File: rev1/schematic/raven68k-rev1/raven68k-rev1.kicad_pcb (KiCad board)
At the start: 4 copper layers, 203.2 x 114.3 mm, 77 parts, among them IC1 L5970D013TR, IC2 L5970D013TR, J1 CPLD_JTAG, J2 DUART_IO, J3 RAPC722BK, SW1 RESET_SW, U1 MCP100-465D, U10 28C256, U11 28C256, U2 68010D, U3 XC9572XL-VQ44, U4 68681, U5 74LS373, U6 CONSOLE, U7 DS12887+, U8 KM684000BLP-7L, U9 KM684000BLP-7L, X1 CLOCK, X2 CXO_DIP14

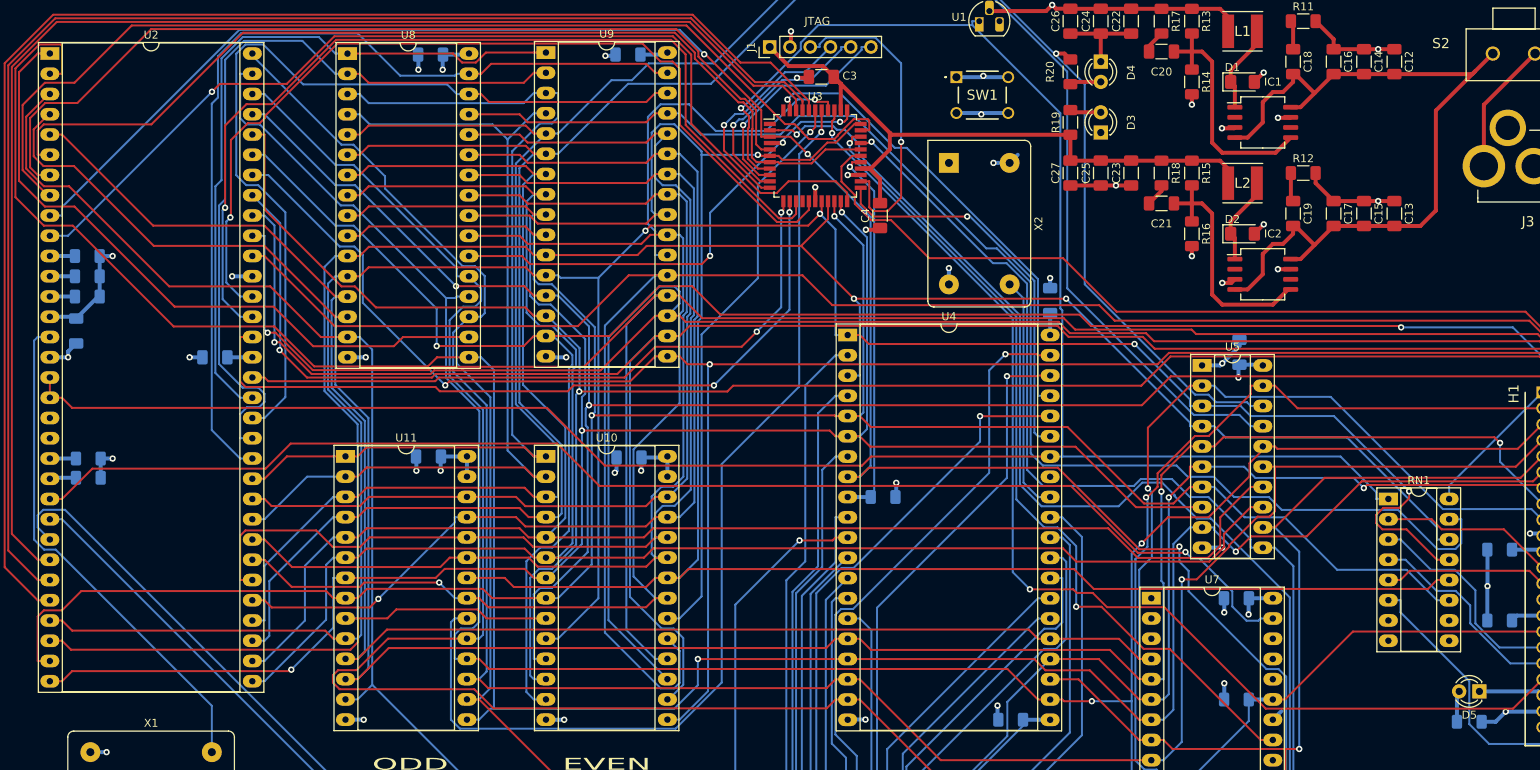
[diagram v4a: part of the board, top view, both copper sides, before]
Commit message: remove tiny leftover traces
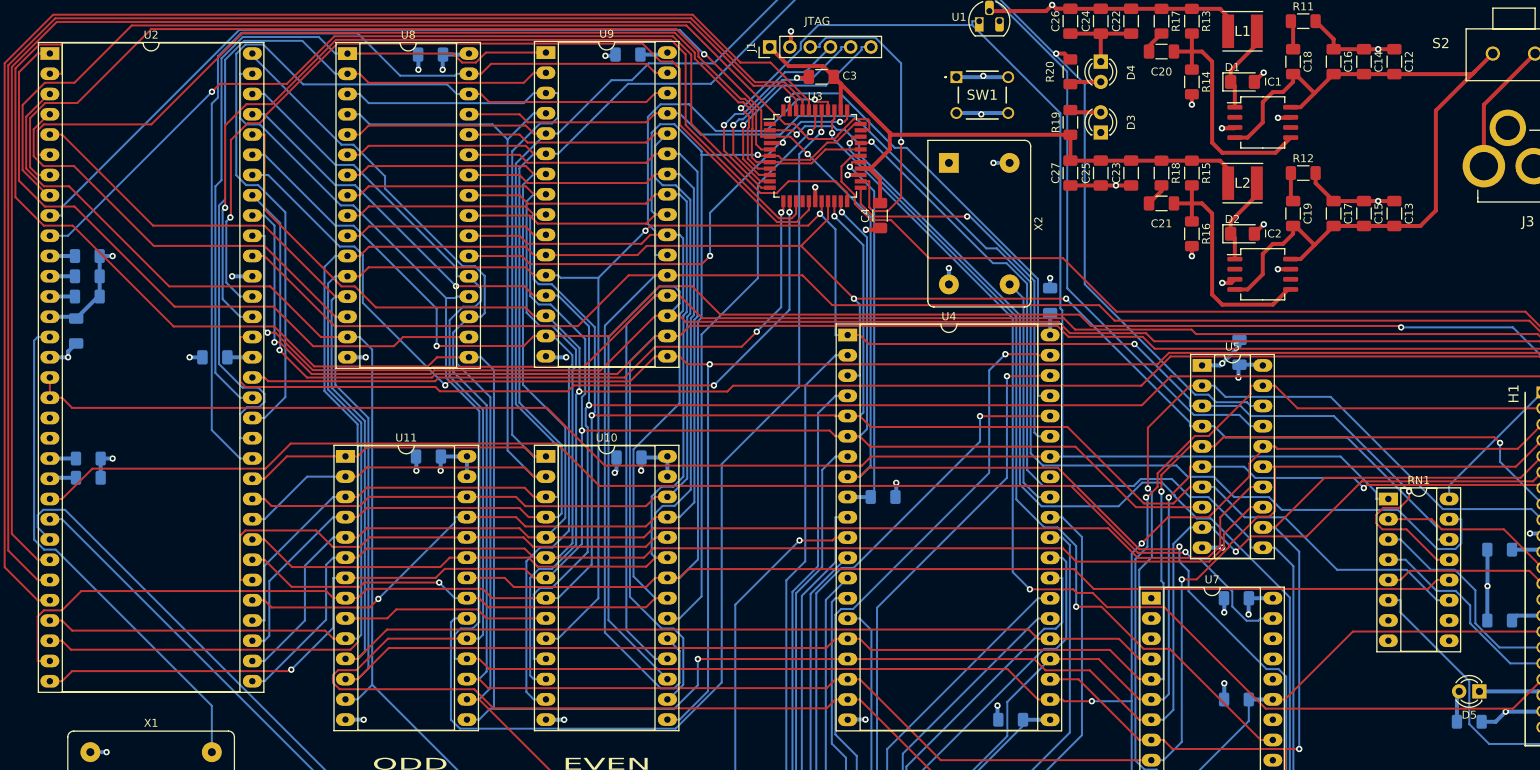
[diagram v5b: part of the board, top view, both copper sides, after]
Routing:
- net +5V: track 133.5 -> 127.0 mm
- net GND: track 147.4 -> 146.6 mm
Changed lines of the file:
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@@
       (layer "B.Cu" (type "copper") (thickness 0.035))
       (layer "B.Mask" (type "Bottom Solder Mask") (thickness 0.01))
+      (layer "B.Paste" (type "Bottom Solder Paste"))
+      (layer "B.SilkS" (type "Bottom Silk Screen"))
       (copper_finish "None")
       (dielectric_constraints no)
@@
       (drillshape 0)
       (scaleselection 1)
-      (outputdirectory "")
+      (outputdirectory "/home/ccureau/git/jani/Raven68k/rev1/gerber/")
     )
   )
@@
   (segment (start 193.0427 74.742) (end 194.173 74.742) (width 0.5) (layer "F.Cu") (net 22))
   (segment (start 173.99 43.4725) (end 177.8 43.4725) (width 0.5) (layer "F.Cu") (net 22))
-  (segment (start 207.29 64.1975) (end 207.01 64.4775) (width 0.5) (layer "F.Cu") (net 22))
   (segment (start 137.871 57.201) (end 137.922 57.15) (width 0.5) (layer "F.Cu") (net 22))
   (segment (start 179.705 62.5225) (end 181.61 62.5225) (width 0.5) (layer "F.Cu") (net 22))
@@
   (via blind (at 68.834 73.914) (size 0.8) (drill 0.4) (layers "In1.Cu" "B.Cu") (net 22))
   (via blind (at 63.5 84.074) (size 0.8) (drill 0.4) (layers "In1.Cu" "B.Cu") (net 22))
-  (segment (start 162.651 53.431) (end 162.814 53.594) (width 0.5) (layer "In2.Cu") (net 22))
-  (segment (start 162.977 53.431) (end 162.814 53.594) (width 0.5) (layer "In2.Cu") (net 22))
   (segment (start 159.691 53.431) (end 162.651 53.431) (width 0.5) (layer "B.Cu") (net 22))
   (segment (start 48.26 84.074) (end 45.979 84.074) (width 0.5) (layer "B.Cu") (net 22))
@@
   (via blind (at 171.704 39.878) (size 0.8) (drill 0.4) (layers "F.Cu" "In2.Cu") (net 25))
   (via blind (at 172.212 45.974) (size 0.8) (drill 0.4) (layers "F.Cu" "In2.Cu") (net 25))
-  (segment (start 163.231 48.931) (end 163.068 48.768) (width 0.5) (layer "In2.Cu") (net 25))
-  (segment (start 162.905 48.931) (end 163.068 48.768) (width 0.5) (layer "In2.Cu") (net 25))
   (via blind (at 164.338 59.69) (size 0.8) (drill 0.4) (layers "In2.Cu" "B.Cu") (net 25))
   (via blind (at 193.294 124.968) (size 0.8) (drill 0.4) (layers "In2.Cu" "B.Cu") (net 25))
@@
   (via blind (at 226.314 112.776) (size 0.8) (drill 0.4) (layers "In2.Cu" "B.Cu") (net 25))
   (segment (start 166.191 48.931) (end 163.231 48.931) (width 0.5) (layer "B.Cu") (net 25))
-  (segment (start 226.648 117.454) (end 226.288 117.094) (width 0.5) (layer "B.Cu") (net 25))
   (segment (start 120.054 46.101) (end 123.185 46.101) (width 0.5) (layer "B.Cu") (net 25))
-  (segment (start 120.054 45.5045) (end 120.054 46.101) (width 0.5) (layer "B.Cu") (net 25))
   (segment (start 196.342 114.338) (end 196.38 114.3) (width 0.5) (layer "B.Cu") (net 25))
   (segment (start 196.3805 114.3) (end 199.38 114.3) (width 0.5) (layer "B.Cu") (net 25))
   (segment (start 233.138 128.524) (end 233.188 128.474) (width 0.5) (layer "B.Cu") (net 25))
-  (segment (start 167.391 58.6695) (end 166.37 59.69) (width 0.5) (layer "B.Cu") (net 25))
   (segment (start 233.188 128.474) (end 235.188 128.474) (width 0.5) (layer "B.Cu") (net 25))
-  (segment (start 49.0555 78.989) (end 49.276 79.2095) (width 0.5) (layer "B.Cu") (net 25))
   (segment (start 227.33 129.794) (end 228.6 128.524) (width 0.5) (layer "B.Cu") (net 25))
   (segment (start 195.072 86.614) (end 195.072 85.1285) (width 0.5) (layer "B.Cu") (net 25))
   (segment (start 152.146 101.499) (end 152.045 101.6) (width 0.5) (layer "B.Cu") (net 25))
   (segment (start 196.342 116.332) (end 196.342 114.338) (width 0.5) (layer "B.Cu") (net 25))
-  (segment (start 184.145 114.295) (end 184.728 114.295) (width 0.5) (layer "B.Cu") (net 25))
   (segment (start 71.369 84.074) (end 71.374 84.069) (width 0.5) (layer "B.Cu") (net 25))
-  (segment (start 199.385 129.535) (end 200.451 128.469) (width 0.5) (layer "B.Cu") (net 25))
-  (segment (start 45.979 78.994) (end 45.974 78.989) (width 0.5) (layer "B.Cu") (net 25))
-  (segment (start 120.054 46.101) (end 120.18 46.228) (width 0.5) (layer "B.Cu") (net 25))
   (segment (start 95.0345 96.52) (end 98.278 96.52) (width 0.5) (layer "B.Cu") (net 25))
   (segment (start 98.42 46.101) (end 98.547 45.974) (width 0.5) (layer "B.Cu") (net 25))
   (segment (start 52.0315 76.454) (end 49.276 79.2095) (width 0.5) (layer "B.Cu") (net 25))
-  (segment (start 49.276 79.2095) (end 49.4675 79.2095) (width 0.5) (layer "B.Cu") (net 25))
   (segment (start 226.314 108.23) (end 226.288 108.204) (width 0.5) (layer "B.Cu") (net 25))
   (segment (start 195.199 85.0015) (end 198.036 85.0015) (width 0.5) (layer "B.Cu") (net 25))
@@
   (segment (start 52.223 76.454) (end 52.0315 76.454) (width 0.5) (layer "B.Cu") (net 25))
   (segment (start 226.314 112.776) (end 226.314 108.23) (width 0.5) (layer "B.Cu") (net 25))
-  (segment (start 120.054 46.101) (end 120.0535 46.101) (width 0.5) (layer "B.Cu") (net 25))
   (segment (start 152.146 99.822) (end 152.146 101.499) (width 0.5) (layer "B.Cu") (net 25))
   (segment (start 164.338 59.69) (end 166.37 59.69) (width 0.5) (layer "B.Cu") (net 25))
   (segment (start 171.45 78.5245) (end 171.45 81.285) (width 0.5) (layer "B.Cu") (net 25))
   (segment (start 120.1805 96.647) (end 123.297 96.647) (width 0.5) (layer "B.Cu") (net 25))
-  (segment (start 171.445 81.28) (end 171.45 81.285) (width 0.5) (layer "B.Cu") (net 25))
   (segment (start 193.294 124.968) (end 193.294 126.974) (width 0.5) (layer "B.Cu") (net 25))
   (segment (start 94.996 96.5585) (end 95.0345 96.52) (width 0.5) (layer "B.Cu") (net 25))
@@
   (segment (start 52.223 71.374) (end 53.848 71.374) (width 0.5) (layer "B.Cu") (net 25))
   (segment (start 196.38 114.3) (end 196.3805 114.3) (width 0.5) (layer "B.Cu") (net 25))
-  (segment (start 120.142 46.1895) (end 120.054 46.101) (width 0.5) (layer "B.Cu") (net 25))
   (segment (start 52.223 71.374) (end 52.223 73.914) (width 0.5) (layer "B.Cu") (net 25))
-  (segment (start 199.385 114.295) (end 199.78 113.9) (width 0.5) (layer "B.Cu") (net 25))
   (segment (start 199.38 114.3) (end 199.385 114.295) (width 0.5) (layer "B.Cu") (net 25))
   (segment (start 164.846 129.439) (end 164.947 129.54) (width 0.5) (layer "B.Cu") (net 25))
@@
   (segment (start 159.691 48.931) (end 162.905 48.931) (width 0.5) (layer "B.Cu") (net 25))
   (segment (start 52.35 99.187) (end 52.35 96.774) (width 0.5) (layer "B.Cu") (net 25))
-  (segment (start 45.969 78.994) (end 45.974 78.989) (width 0.5) (layer "B.Cu") (net 25))
   (segment (start 120.18 98.2595) (end 120.18 96.647) (width 0.5) (layer "B.Cu") (net 25))
   (segment (start 45.974 78.989) (end 49.0555 78.989) (width 0.5) (layer "B.Cu") (net 25))
@@
   (segment (start 150.114 64.7315) (end 150.114 61.705) (width 0.5) (layer "F.Cu") (net 66))
   (segment (start 189.23 59.41) (end 185.42 59.41) (width 0.5) (layer "F.Cu") (net 66))
-  (segment (start 173.837 56.007) (end 173.99 56.16) (width 0.5) (layer "F.Cu") (net 66))
   (segment (start 148.81 60.401) (end 148.936 60.401) (width 0.5) (layer "F.Cu") (net 66))
   (segment (start 173.99 59.3975) (end 173.99 56.16) (width 0.5) (layer "F.Cu") (net 66))
@@
   (segment (start 201.65 64.1975) (end 201.93 64.4775) (width 0.5) (layer "F.Cu") (net 82))
   (segment (start 201.65 60.96) (end 201.65 64.1975) (width 0.5) (layer "F.Cu") (net 82))
-  (segment (start 186.982 45.72) (end 186.9825 45.72) (width 0.5) (layer "F.Cu") (net 83))
   (segment (start 189.23 43.46) (end 189.23 45.72) (width 0.5) (layer "F.Cu") (net 83))
   (segment (start 193.04 58.42) (end 191.77 57.15) (width 0.5) (layer "F.Cu") (net 83))
@@
   (segment (start 193.04 77.47) (end 191.77 76.2) (width 0.5) (layer "F.Cu") (net 85))
   (segment (start 190.5 64.77) (end 189.23 64.77) (width 0.5) (layer "F.Cu") (net 85))
-  (segment (start 186.982 64.77) (end 186.9825 64.77) (width 0.5) (layer "F.Cu") (net 85))
   (segment (start 199.39 77.47) (end 193.04 77.47) (width 0.5) (layer "F.Cu") (net 85))
   (segment (start 186.9825 64.77) (end 189.23 64.77) (width 0.5) (layer "F.Cu") (net 85))
@@
   (segment (start 225.298 125.984) (end 232.698 125.984) (width 0.5) (layer "B.Cu") (net 134))
   (segment (start 174.27 53.34) (end 177.8 53.34) (width 0.5) (layer "F.Cu") (net 135))
-  (segment (start 173.99 53.06) (end 174.27 53.34) (width 0.15) (layer "F.Cu") (net 135))
   (segment (start 174.27 49.53) (end 177.8 49.53) (width 0.5) (layer "F.Cu") (net 136))
   (segment (start 173.99 49.81) (end 174.27 49.53) (width 0.15) (layer "F.Cu") (net 136))

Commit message: some helpful labels
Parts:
- added C28: 0.1uF, Capacitor_SMD:C_1206_3216Metric_Pad1.33x1.80mm_HandSolder, F.Cu at (156.5, 40.9)
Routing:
- net +5V: track 127.0 -> 132.9 mm
- net GND: track 146.6 -> 148.3 mm, vias 41 -> 42
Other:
- board text added: "IP0-5"
- board text added: "JLCJLCJLCJLC"
- board text added: "OP0-7"
- board text added: "Order No."
- board text added: "PATA IDE"
- board text added: "RESET"
- board text added: "RxA"
- board text added: "RxB"
- board text added: "The Raven68k (Rev 1, 2022-02-09) https://github.com/jkuituni/Raven68k"
- board text added: "TxA"
- board text added: "TxB"
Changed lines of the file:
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@@
+    )
+  )
+  (footprint "Capacitor_SMD:C_1206_3216Metric_Pad1.33x1.80mm_HandSolder" (layer "F.Cu")
+    (at 156.464 40.894)
+    (descr "Capacitor SMD 1206 (3216 Metric), square (rectangular) end terminal, IPC_7351 nominal with elongated pad for handsoldering. (Body size source: IPC-SM-782 page 76, https://www.pcb-3d.com/wordpress/wp-content/uploads/ipc-sm-782a_amendment_1_and_2.pdf), generated with kicad-footprint-generator")
+    (tags "capacitor handsolder")
+    (property "Sheetfile" "raven68k-rev1.kicad_sch")
+    (property "Sheetname" "")
+    (attr smd)
+    (fp_text reference "C28" (at 0 -1.85) (layer "F.SilkS")
+      (effects (font (size 1 1) (thickness 0.15)))
+    )
+    (fp_text value "0.1uF" (at 0 1.85) (layer "F.Fab")
+      (effects (font (size 1 1) (thickness 0.15)))
+    )
+    (fp_text user "${REFERENCE}" (at 0 0) (layer "F.Fab")
+      (effects (font (size 0.8 0.8) (thickness 0.12)))
+    )
+    (fp_line (start -0.711252 0.91) (end 0.711252 0.91) (layer "F.SilkS") (width 0.12))
+    (fp_line (start -0.711252 -0.91) (end 0.711252 -0.91) (layer "F.SilkS") (width 0.12))
+    (fp_line (start -2.48 1.15) (end -2.48 -1.15) (layer "F.CrtYd") (width 0.05))
+    (fp_line (start 2.48 1.15) (end -2.48 1.15) (layer "F.CrtYd") (width 0.05))
+    (fp_line (start 2.48 -1.15) (end 2.48 1.15) (layer "F.CrtYd") (width 0.05))
+    (fp_line (start -2.48 -1.15) (end 2.48 -1.15) (layer "F.CrtYd") (width 0.05))
+    (fp_line (start 1.6 -0.8) (end 1.6 0.8) (layer "F.Fab") (width 0.1))
+    (fp_line (start 1.6 0.8) (end -1.6 0.8) (layer "F.Fab") (width 0.1))
+    (fp_line (start -1.6 -0.8) (end 1.6 -0.8) (layer "F.Fab") (width 0.1))
+    (fp_line (start -1.6 0.8) (end -1.6 -0.8) (layer "F.Fab") (width 0.1))
+    (pad "1" smd roundrect (at -1.5625 0) (size 1.325 1.8) (layers "F.Cu" "F.Paste" "F.Mask") (roundrect_rratio 0.188679)
+      (net 22 "GND") (pintype "passive"))
+    (pad "2" smd roundrect (at 1.5625 0) (size 1.325 1.8) (layers "F.Cu" "F.Paste" "F.Mask") (roundrect_rratio 0.188679)
+      (net 25 "+5V") (pintype "passive"))
+    (model "${KICAD6_3DMODEL_DIR}/Capacitor_SMD.3dshapes/C_1206_3216Metric.wrl"
+      (offset (xyz 0 0 0))
+      (scale (xyz 1 1 1))
+      (rotate (xyz 0 0 0))
     )
   )
@@
     (descr "Capacitor SMD 1206 (3216 Metric), square (rectangular) end terminal, IPC_7351 nominal with elongated pad for handsoldering. (Body size source: IPC-SM-782 page 76, https://www.pcb-3d.com/wordpress/wp-content/uploads/ipc-sm-782a_amendment_1_and_2.pdf), generated with kicad-footprint-generator")
     (tags "capacitor handsolder")
+    (property "LCSC" "C24497")
     (property "Sheetfile" "DUART.kicad_sch")
     (property "Sheetname" "DUART and RTC")
@@
   (gr_line (start 241.3 152.4) (end 38.1 152.4) (layer "Edge.Cuts") (width 0.05))
   (gr_line (start 38.1 38.1) (end 241.3 38.1) (layer "Edge.Cuts") (width 0.05))
-  (gr_text "ODD" (at 91.186 135.128) (layer "F.SilkS")
+  (gr_text "Order No. " (at 66.04 149.86) (layer "B.SilkS")
+    (effects (font (size 1.5 1.5) (thickness 0.3)) (justify mirror))
+  )
+  (gr_text "JLCJLCJLCJLC" (at 52.578 149.86) (layer "B.SilkS")
+    (effects (font (size 1.5 1.5) (thickness 0.3)) (justify mirror))
+  )
+  (gr_text "RESET" (at 163.068 46.482) (layer "F.SilkS")
+    (effects (font (size 1 1) (thickness 0.15)))
+  )
+  (gr_text "OP0-7" (at 140.97 146.812) (layer "F.SilkS")
+    (effects (font (size 1 1) (thickness 0.15)))
+  )
+  (gr_text "The Raven68k (Rev 1, 2022-02-09) https://github.com/jkuituni/Raven68k" (at 209.042 149.606) (layer "F.SilkS")
+    (effects (font (size 1 1) (thickness 0.15)))
+  )
+  (gr_text "RxB" (at 134.366 138.684 90) (layer "F.SilkS")
+    (effects (font (size 1 1) (thickness 0.15)))
+  )
+  (gr_text "IP0-5" (at 144.78 139.192) (layer "F.SilkS")
+    (effects (font (size 1 1) (thickness 0.15)))
+  )
+  (gr_text "TxB" (at 132.08 138.684 90) (layer "F.SilkS")
+    (effects (font (size 1 1) (thickness 0.15)))
+  )
+  (gr_text "ODD" (at 91.186 134.874) (layer "F.SilkS")
     (effects (font (size 1.5 3) (thickness 0.3)))
   )
-  (gr_text "EVEN" (at 115.824 135.128) (layer "F.SilkS")
+  (gr_text "EVEN" (at 115.824 134.874) (layer "F.SilkS")
     (effects (font (size 1.5 3) (thickness 0.3)))
   )
   (gr_text "JTAG" (at 142.24 41.91) (layer "F.SilkS")
     (effects (font (size 1 1) (thickness 0.15)))
+  )
+  (gr_text "RxA" (at 168.402 145.796 90) (layer "F.SilkS")
+    (effects (font (size 1 1) (thickness 0.15)))
+  )
+  (gr_text "TxA" (at 165.862 145.796 90) (layer "F.SilkS")
+    (effects (font (size 1 1) (thickness 0.15)))
+  )
+  (gr_text "PATA IDE" (at 228.854 106.426 90) (layer "F.SilkS")
+    (effects (font (size 1.5 1.5) (thickness 0.3)))
   )
   (segment (start 187.9624 111.9331) (end 189.8336 111.9331) (width 0.25) (layer "F.Cu") (net 1))
@@
   (segment (start 189.23 71.3852) (end 189.23 70.13) (width 0.5) (layer "F.Cu") (net 22))
   (segment (start 141.986 64.501) (end 141.986 62.738) (width 0.5) (layer "F.Cu") (net 22))
+  (segment (start 153.162 40.894) (end 154.9015 40.894) (width 0.25) (layer "F.Cu") (net 22))
   (segment (start 148.336 68.072) (end 149.898 68.072) (width 0.5) (layer "F.Cu") (net 22))
   (segment (start 210.82 45.4275) (end 212.6031 45.4275) (width 0.5) (layer "F.Cu") (net 22))
@@
   (via (at 212.6031 45.4275) (size 0.8) (drill 0.4) (layers "F.Cu" "B.Cu") (net 22))
   (via blind (at 148.336 68.072) (size 0.8) (drill 0.4) (layers "F.Cu" "In1.Cu") (net 22))
+  (via blind (at 153.162 40.894) (size 0.8) (drill 0.4) (layers "F.Cu" "In1.Cu") (free) (net 22))
   (via (at 171.45 74.1353) (size 0.8) (drill 0.4) (layers "F.Cu" "B.Cu") (net 22))
   (via (at 193.0427 74.742) (size 0.8) (drill 0.4) (layers "F.Cu" "B.Cu") (net 22))
@@
   (segment (start 185.42 40.36) (end 181.6141 40.36) (width 0.5) (layer "F.Cu") (net 25))
   (segment (start 173.254 45.974) (end 173.99 46.71) (width 0.5) (layer "F.Cu") (net 25))
+  (segment (start 158.0265 40.894) (end 158.2805 40.64) (width 0.25) (layer "F.Cu") (net 25))
   (segment (start 172.212 45.974) (end 173.254 45.974) (width 0.5) (layer "F.Cu") (net 25))
+  (segment (start 158.2805 40.64) (end 163.83 40.64) (width 0.25) (layer "F.Cu") (net 25))
   (segment (start 163.83 40.64) (end 170.942 40.64) (width 0.5) (layer "F.Cu") (net 25))
   (segment (start 177.8 40.3519) (end 177.8 40.3475) (width 0.5) (layer "F.Cu") (net 25))
